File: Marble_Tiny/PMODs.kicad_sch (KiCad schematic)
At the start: 6 parts, among them J14 Conn_02x06_Odd_Even, J15 Conn_02x06_Odd_Even, J4 Conn_02x06_Odd_Even, J5 Conn_02x06_Odd_Even, J6 Conn_02x06_Odd_Even, J7 Conn_02x06_Odd_Even

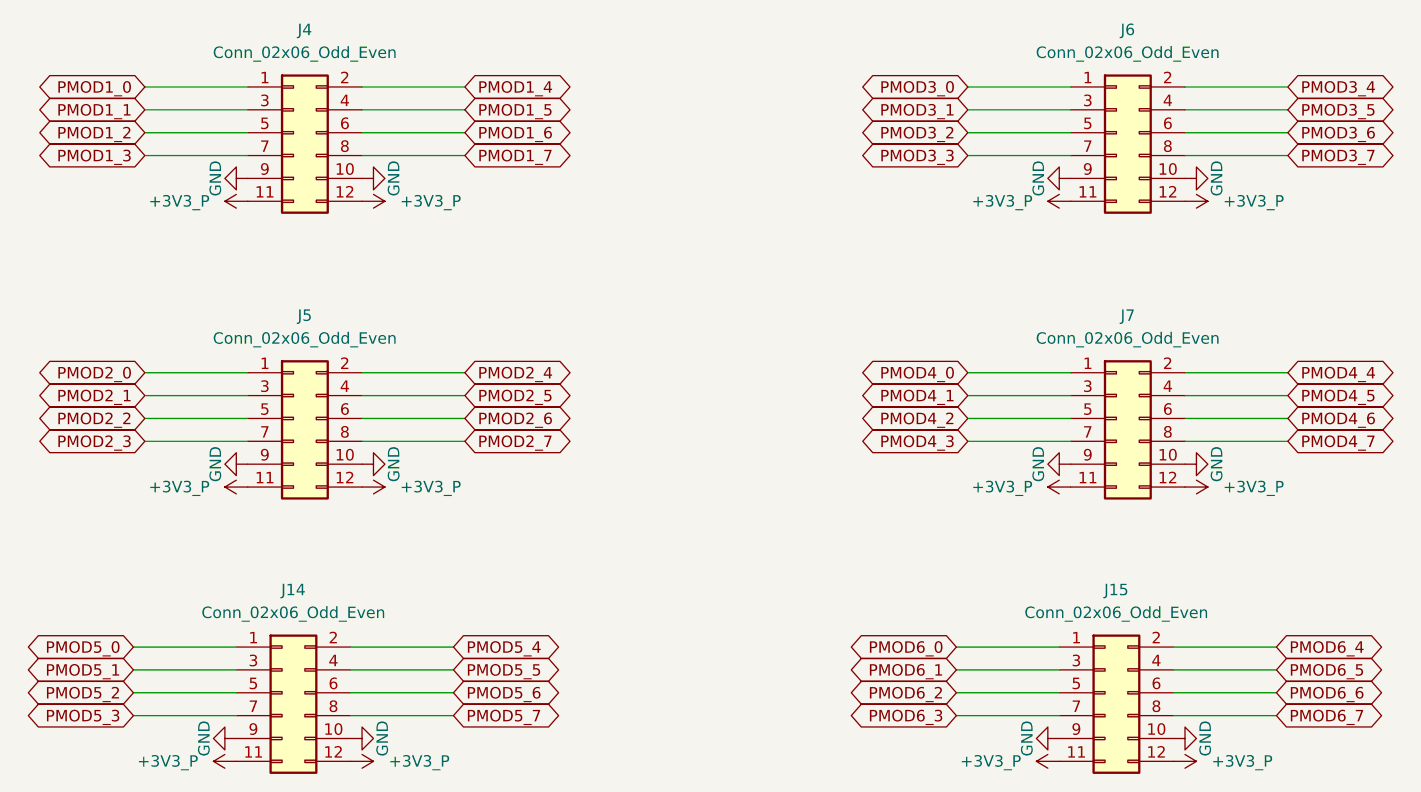
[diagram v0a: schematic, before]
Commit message: fixed issue with PMODs; added board name and revision; fixed polygons issue
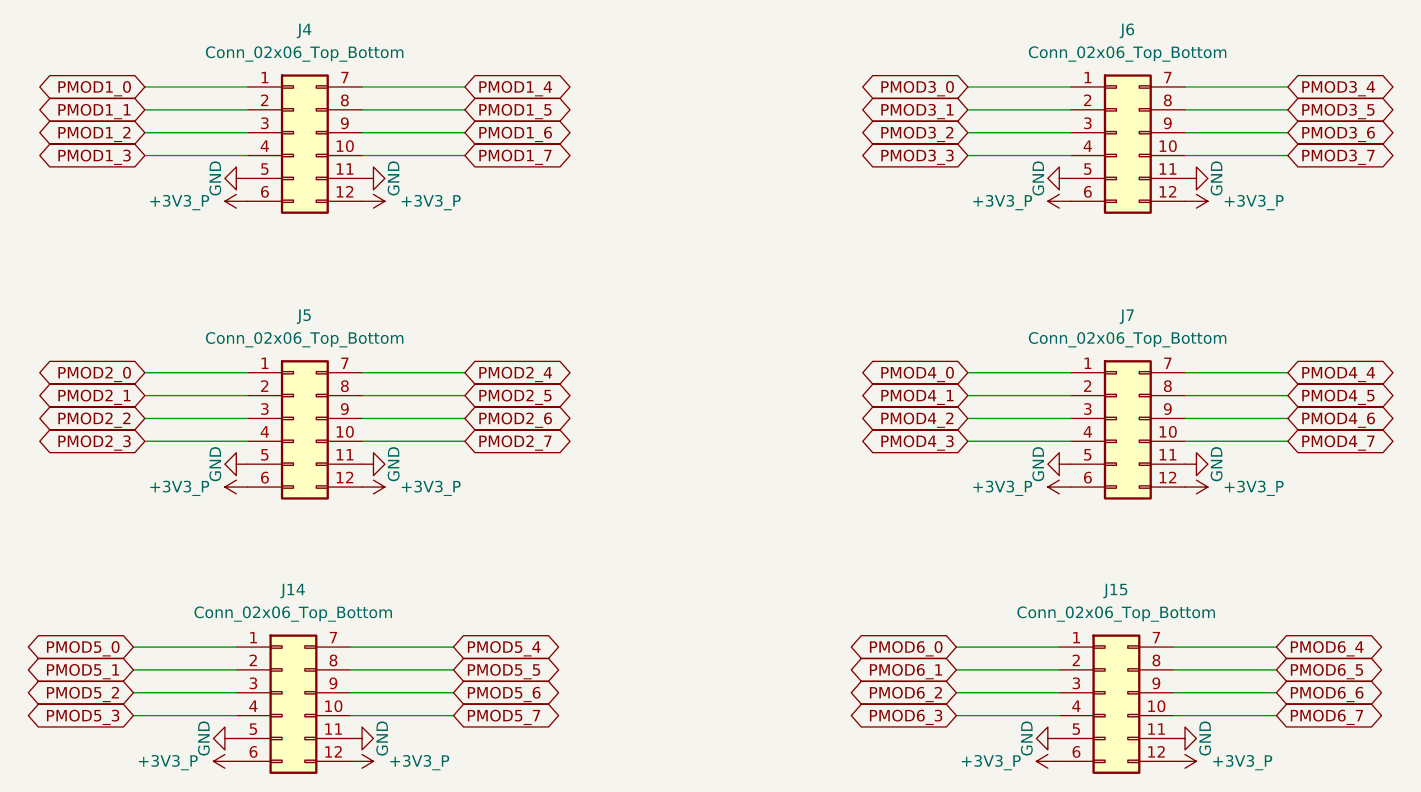
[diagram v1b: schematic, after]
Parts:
- removed J14, J15: Conn_02x06_Odd_Even, Connector_PinSocket_2.54mm:PinSocket_2x06_P2.54mm_Vertical, symbol Connector_Generic:Conn_02x06_Odd_Even
- removed J4, J5, J6, J7: Conn_02x06_Odd_Even, Connector_PinSocket_2.54mm:PinSocket_2x06_P2.54mm_Horizontal, symbol Connector_Generic:Conn_02x06_Odd_Even
- added J15: Conn_02x06_Top_Bottom, Miscellaneous THD:PinSocket_2x06_P2.54mm_Vertical_PMOD, symbol Connector_Generic:Conn_02x06_Top_Bottom
- added J4, J5, J6, J7: Conn_02x06_Top_Bottom, Miscellaneous THD:PinSocket_2x06_P2.54mm_Horizontal_PMOD, symbol Connector_Generic:Conn_02x06_Top_Bottom
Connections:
- net +3V3_P: now also J15.12 (Pin_12), J15.6 (Pin_6), J4.12 (Pin_12), J4.6 (Pin_6), J5.12 (Pin_12), J5.6 (Pin_6), J6.12 (Pin_12), J6.6 (Pin_6), J7.12 (Pin_12), J7.6 (Pin_6)
- net GND: now also J15.11 (Pin_11), J15.5 (Pin_5), J4.11 (Pin_11), J4.5 (Pin_5), J5.11 (Pin_11), J5.5 (Pin_5), J6.11 (Pin_11), J6.5 (Pin_5), J7.11 (Pin_11), J7.5 (Pin_5)
- net PMOD1_0: now also J4.1 (Pin_1)
- net PMOD1_1: now also J4.2 (Pin_2)
- net PMOD1_2: now also J4.3 (Pin_3)
- net PMOD1_3: now also J4.4 (Pin_4)
- net PMOD1_4: now also J4.7 (Pin_7)
- net PMOD1_5: now also J4.8 (Pin_8)
- net PMOD1_6: now also J4.9 (Pin_9)
- net PMOD1_7: now also J4.10 (Pin_10)
- net PMOD2_0: now also J5.1 (Pin_1)
- net PMOD2_1: now also J5.2 (Pin_2)
- net PMOD2_2: now also J5.3 (Pin_3)
- net PMOD2_3: now also J5.4 (Pin_4)
- net PMOD2_4: now also J5.7 (Pin_7)
- net PMOD2_5: now also J5.8 (Pin_8)
- net PMOD2_6: now also J5.9 (Pin_9)
- net PMOD2_7: now also J5.10 (Pin_10)
- net PMOD3_0: now also J6.1 (Pin_1)
- net PMOD3_1: now also J6.2 (Pin_2)
- net PMOD3_2: now also J6.3 (Pin_3)
- net PMOD3_3: now also J6.4 (Pin_4)
- net PMOD3_4: now also J6.7 (Pin_7)
- net PMOD3_5: now also J6.8 (Pin_8)
- net PMOD3_6: now also J6.9 (Pin_9)
- net PMOD3_7: now also J6.10 (Pin_10)
- net PMOD4_0: now also J7.1 (Pin_1)
- net PMOD4_1: now also J7.2 (Pin_2)
- net PMOD4_2: now also J7.3 (Pin_3)
- net PMOD4_3: now also J7.4 (Pin_4)
- net PMOD4_4: now also J7.7 (Pin_7)
- net PMOD4_5: now also J7.8 (Pin_8)
- net PMOD4_6: now also J7.9 (Pin_9)
- net PMOD4_7: now also J7.10 (Pin_10)
- net PMOD5_0: now also J15.1 (Pin_1)
- net PMOD5_1: now also J15.2 (Pin_2)
- net PMOD5_2: now also J15.3 (Pin_3)
- net PMOD5_3: now also J15.4 (Pin_4)
- net PMOD5_4: now also J15.7 (Pin_7)
- net PMOD5_5: now also J15.8 (Pin_8)
- net PMOD5_6: now also J15.9 (Pin_9)
- net PMOD5_7: now also J15.10 (Pin_10)
- net PMOD6_0: now also J15.1 (Pin_1)
- net PMOD6_1: now also J15.2 (Pin_2)
- net PMOD6_2: now also J15.3 (Pin_3)
- net PMOD6_3: now also J15.4 (Pin_4)
- net PMOD6_4: now also J15.7 (Pin_7)
- net PMOD6_5: now also J15.8 (Pin_8)
- net PMOD6_6: now also J15.9 (Pin_9)
- net PMOD6_7: now also J15.10 (Pin_10)
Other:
- company: (none) -> ${name}
